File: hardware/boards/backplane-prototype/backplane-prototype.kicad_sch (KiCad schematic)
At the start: 32 parts, among them J1 DC_IN, J2 SLOT_1, J3 SLOT_2, J4 SLOT_3, J5 SLOT_4, J6 SLOT_5, J7 SLOT_6, J8 i2c_busses

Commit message: chore: checkpoint current board layout
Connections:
- net SCL_SLOT_1: now also D3.1 (IO1); no longer D3.2 (IO2)
- net SCL_SLOT_2: now also D4.1 (IO1); no longer D4.2 (IO2)
- net SCL_SLOT_3: now also D5.1 (IO1); no longer D5.2 (IO2)
- net SCL_SLOT_4: now also D6.1 (IO1); no longer D6.2 (IO2)
- net SCL_SLOT_5: now also D7.1 (IO1); no longer D7.2 (IO2)
- net SCL_SLOT_6: now also D8.1 (IO1); no longer D8.2 (IO2)
- net SDA_SLOT_1: now also D3.2 (IO2); no longer D3.1 (IO1)
- net SDA_SLOT_2: now also D4.2 (IO2); no longer D4.1 (IO1)
- net SDA_SLOT_3: now also D5.2 (IO2); no longer D5.1 (IO1)
- net SDA_SLOT_4: now also D6.2 (IO2); no longer D6.1 (IO1)
- net SDA_SLOT_5: now also D7.2 (IO2); no longer D7.1 (IO1)
- net SDA_SLOT_6: now also D8.2 (IO2); no longer D8.1 (IO1)
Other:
- title: Simplified XT30 Backplane Prototype -> Backplane Prototype
- moved on the sheet: J1, R10, R11, R12, R13, R14, R3, R4, R5, R6, R7, R8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

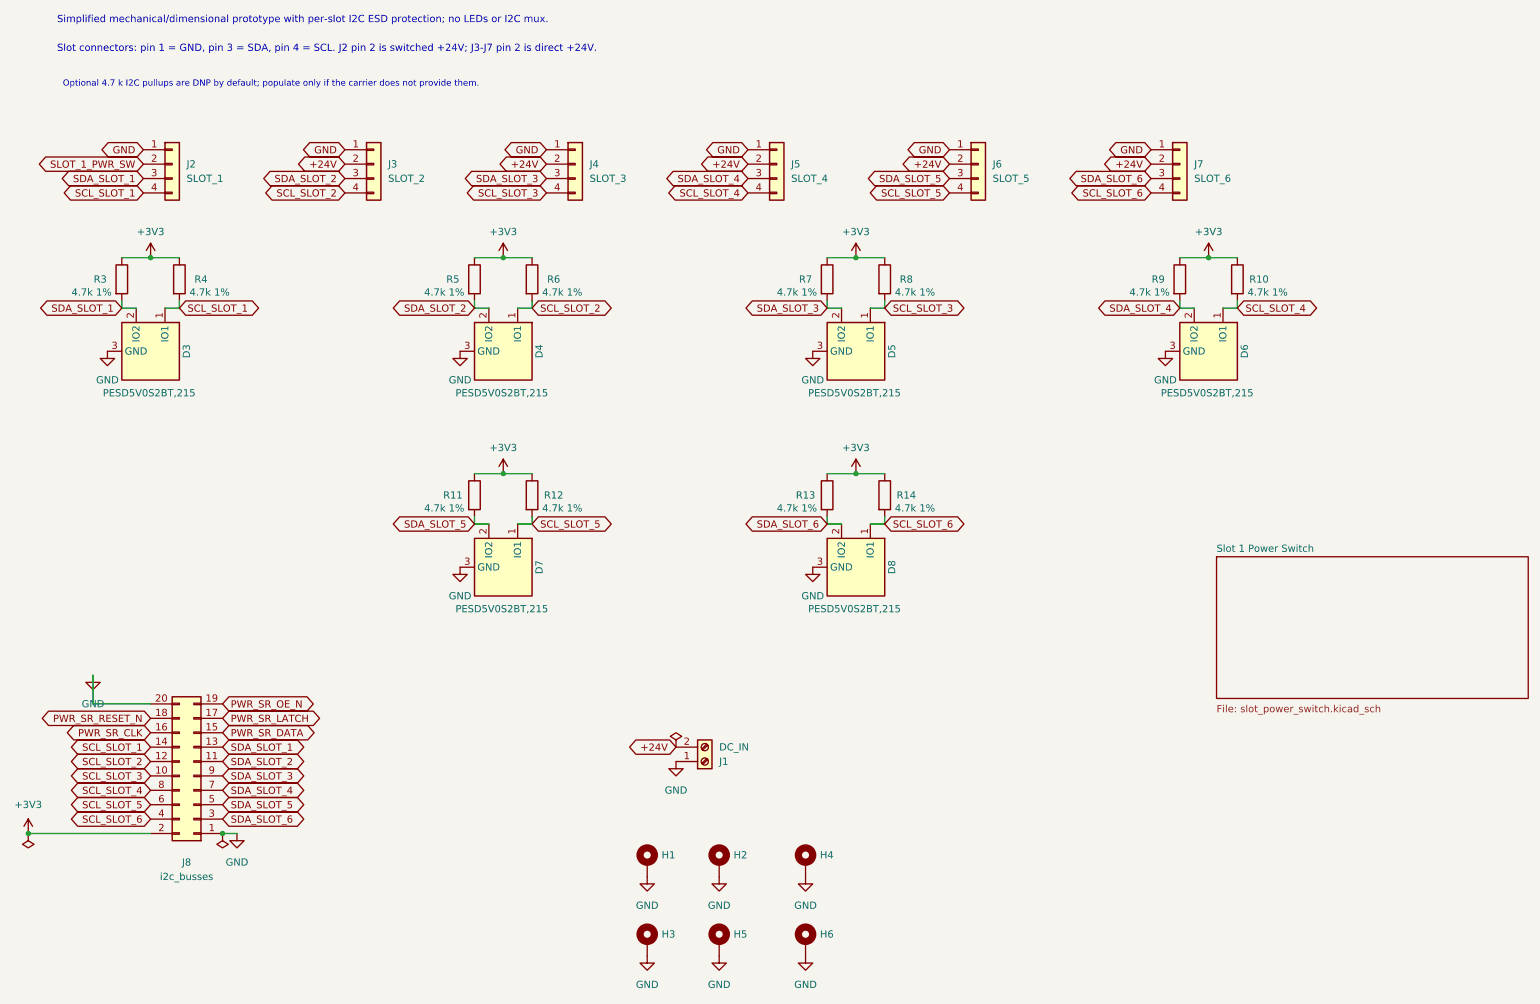
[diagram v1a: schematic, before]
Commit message: feat: add power switches for all backplane slots
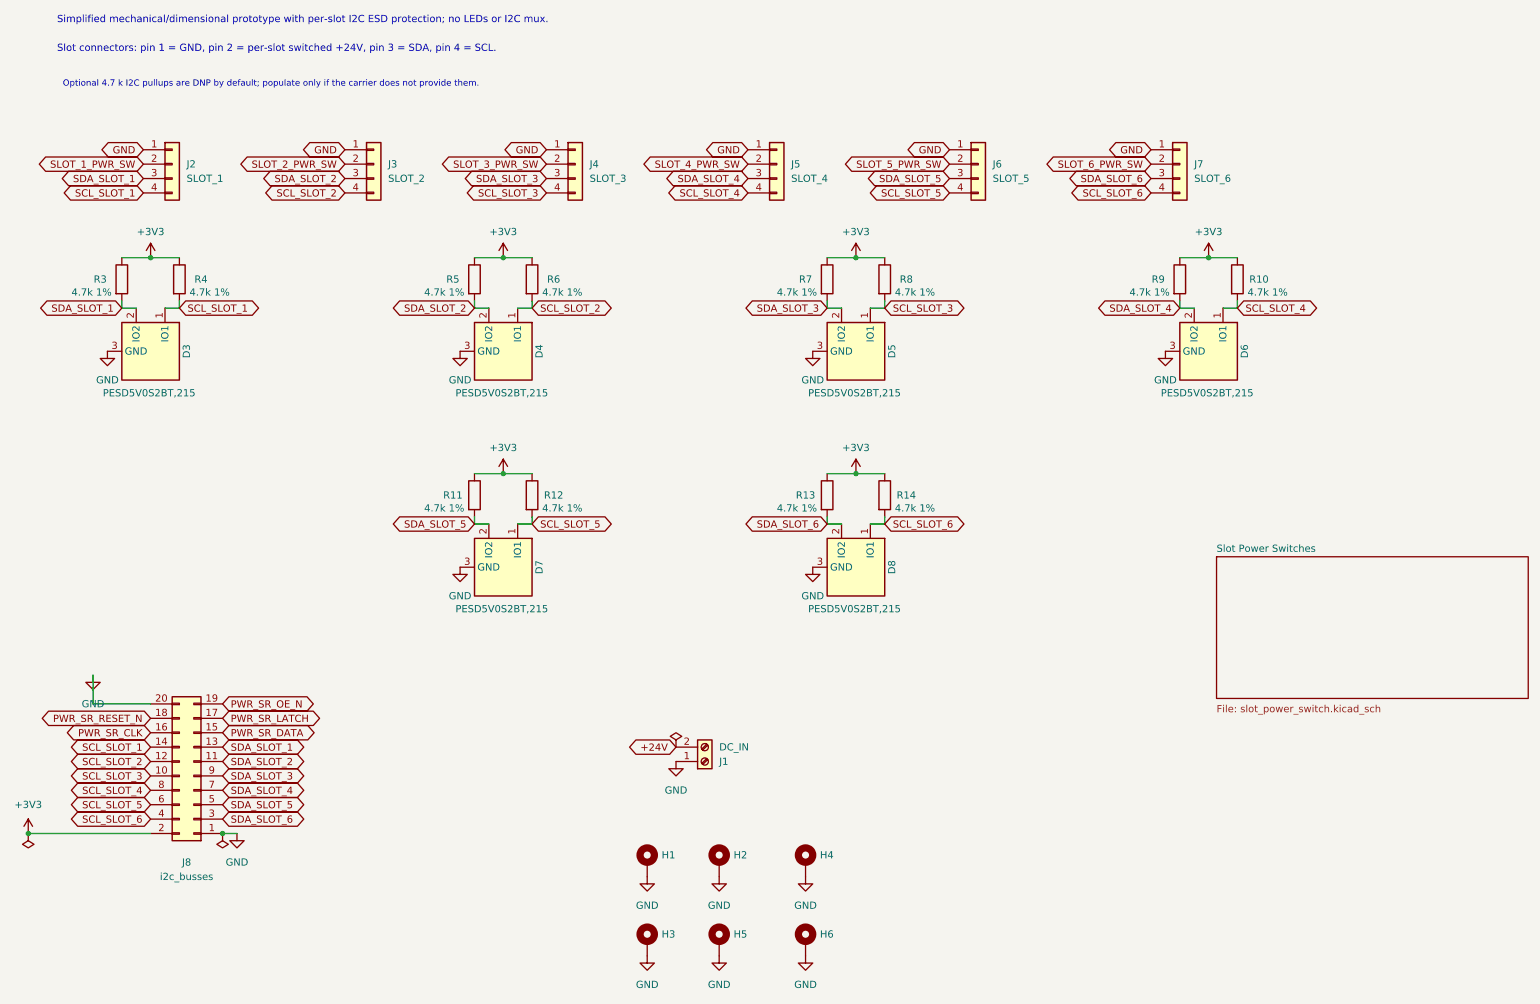
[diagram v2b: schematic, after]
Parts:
- J3: Pinout 1=GND; 2=+24V; 3=SDA; 4=SCL -> 1=GND; 2=SLOT_2_PWR_SW; 3=SDA; 4=SCL
- J4: Pinout 1=GND; 2=+24V; 3=SDA; 4=SCL -> 1=GND; 2=SLOT_3_PWR_SW; 3=SDA; 4=SCL
- J5: Pinout 1=GND; 2=+24V; 3=SDA; 4=SCL -> 1=GND; 2=SLOT_4_PWR_SW; 3=SDA; 4=SCL
- J6: Pinout 1=GND; 2=+24V; 3=SDA; 4=SCL -> 1=GND; 2=SLOT_5_PWR_SW; 3=SDA; 4=SCL
- J7: Pinout 1=GND; 2=+24V; 3=SDA; 4=SCL -> 1=GND; 2=SLOT_6_PWR_SW; 3=SDA; 4=SCL
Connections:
- net +24V: no longer J3.2 (Pin_2), J4.2 (Pin_2), J5.2 (Pin_2), J6.2 (Pin_2), J7.2 (Pin_2)
- new net SLOT_2_PWR_SW: J3.2 (Pin_2)
- new net SLOT_3_PWR_SW: J4.2 (Pin_2)
- new net SLOT_4_PWR_SW: J5.2 (Pin_2)
- new net SLOT_5_PWR_SW: J6.2 (Pin_2)
- new net SLOT_6_PWR_SW: J7.2 (Pin_2)
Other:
- sheet Slot 1 Power Switch renamed Slot Power Switches
- note added: "Slot connectors: pin 1 = GND, pin 2 = per-slot switched +24V, pin 3 = SDA, pin 4 = SCL."
- note removed: "Slot connectors: pin 1 = GND, pin 3 = SDA, pin 4 = SCL. J2 pin 2 is switched +24V; J3-J7 pin 2 is direct +24V."
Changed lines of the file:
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@@
 		)
 	)
-	(text "Slot connectors: pin 1 = GND, pin 3 = SDA, pin 4 = SCL. J2 pin 2 is switched +24V; J3-J7 pin 2 is direct +24V."
+	(text "Slot connectors: pin 1 = GND, pin 2 = per-slot switched +24V, pin 3 = SDA, pin 4 = SCL."
 		(exclude_from_sim no)
 		(at 25.4 25.4 0)
@@
 		)
 	)
-	(global_label "+24V"
+	(global_label "SLOT_3_PWR_SW"
 		(shape bidirectional)
 		(at 111.76 45.72 180)
@@
 		)
 	)
-	(global_label "+24V"
+	(global_label "SLOT_5_PWR_SW"
 		(shape bidirectional)
 		(at 182.88 45.72 180)
@@
 		)
 	)
-	(global_label "+24V"
+	(global_label "SLOT_4_PWR_SW"
 		(shape bidirectional)
 		(at 147.32 45.72 180)
@@
 		)
 	)
-	(global_label "+24V"
+	(global_label "SLOT_2_PWR_SW"
 		(shape bidirectional)
 		(at 76.2 45.72 180)
@@
 		)
 	)
-	(global_label "+24V"
+	(global_label "SLOT_6_PWR_SW"
 		(shape bidirectional)
 		(at 218.44 45.72 180)
@@
 			)
 		)
-		(property "Pinout" "1=GND; 2=+24V; 3=SDA; 4=SCL"
+		(property "Pinout" "1=GND; 2=SLOT_6_PWR_SW; 3=SDA; 4=SCL"
 			(at 223.52 45.72 0)
 			(hide yes)
@@
 			)
 		)
-		(property "Pinout" "1=GND; 2=+24V; 3=SDA; 4=SCL"
+		(property "Pinout" "1=GND; 2=SLOT_3_PWR_SW; 3=SDA; 4=SCL"
 			(at 116.84 45.72 0)
 			(hide yes)
@@
 			)
 		)
-		(property "Pinout" "1=GND; 2=+24V; 3=SDA; 4=SCL"
+		(property "Pinout" "1=GND; 2=SLOT_5_PWR_SW; 3=SDA; 4=SCL"
 			(at 187.96 45.72 0)
 			(hide yes)
@@
 			)
 		)
-		(property "Pinout" "1=GND; 2=+24V; 3=SDA; 4=SCL"
+		(property "Pinout" "1=GND; 2=SLOT_2_PWR_SW; 3=SDA; 4=SCL"
 			(at 81.28 45.72 0)
 			(hide yes)
@@
 			)
 		)
-		(property "Pinout" "1=GND; 2=+24V; 3=SDA; 4=SCL"
+		(property "Pinout" "1=GND; 2=SLOT_4_PWR_SW; 3=SDA; 4=SCL"
 			(at 152.4 45.72 0)
 			(hide yes)
@@
 			(color 0 0 0 0)
 		)
-		(property "Sheetname" "Slot 1 Power Switch"
+		(property "Sheetname" "Slot Power Switches"
 			(at 230 114.2884 0)
 			(show_name no)

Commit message: feat: replace backplane input terminal
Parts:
- J1: footprint mini-rack-power:DEGSON_DG135T-10.16-02P -> mini-rack-power:DORABO_DB910-6.35-2P-GN-S; LCSC (none) -> C395872; MPN (none) -> DB910-6.35-2P-GN-S; Manufacturer (none) -> DORABO
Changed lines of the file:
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@@
 			)
 		)
-		(property "Footprint" "mini-rack-power:DEGSON_DG135T-10.16-02P"
+		(property "Footprint" "mini-rack-power:DORABO_DB910-6.35-2P-GN-S"
 			(at 139.7 151.13 0)
 			(hide yes)
@@
 			)
 		)
-		(property "Datasheet" ""
+		(property "Datasheet" "https://www.lcsc.com/datasheet/C395872.pdf"
 			(at 139.7 151.13 0)
 			(hide yes)
@@
 			)
 		)
-		(property "Description" "Prototype main DC input screw terminal"
+		(property "Description" "DORABO DB910-6.35-2P-GN-S, 2-position 6.35 mm pitch vertical screw terminal, LCSC C395872"
 			(at 139.7 151.13 0)
 			(hide yes)
@@
 			(at 139.7 151.13 0)
 			(hide yes)
+			(show_name no)
+			(do_not_autoplace no)
+			(effects
+				(font
+					(size 1.27 1.27)
+				)
+			)
+		)
+		(property "MPN" "DB910-6.35-2P-GN-S"
+			(at 139.7 151.13 0)
+			(hide yes)
+			(show_name no)
+			(do_not_autoplace no)
+			(effects
+				(font
+					(size 1.27 1.27)
+				)
+			)
+		)
+		(property "LCSC" "C395872"
+			(at 139.7 151.13 0)
+			(hide yes)
+			(show_name no)
+			(do_not_autoplace no)
+			(effects
+				(font
+					(size 1.27 1.27)
+				)
+			)
+		)
+		(property "Manufacturer" "DORABO"
+			(at 139.7 151.13 0)
+			(hide yes)

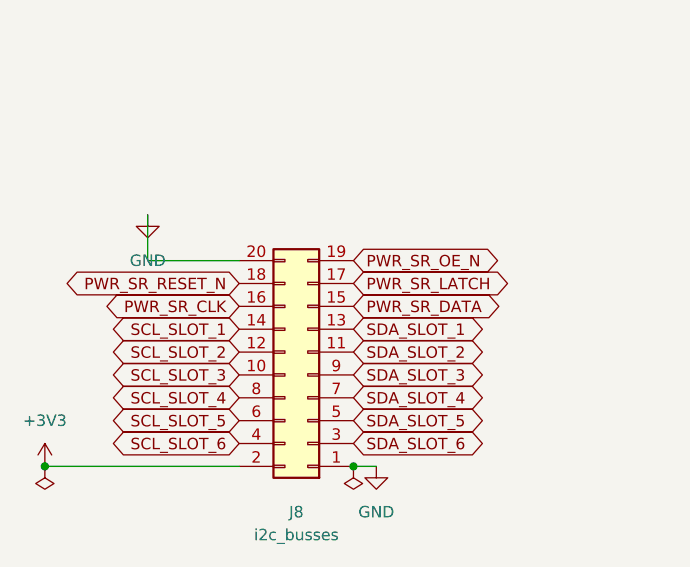
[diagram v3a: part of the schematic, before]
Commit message: Replace slot power shift register with PCA9554
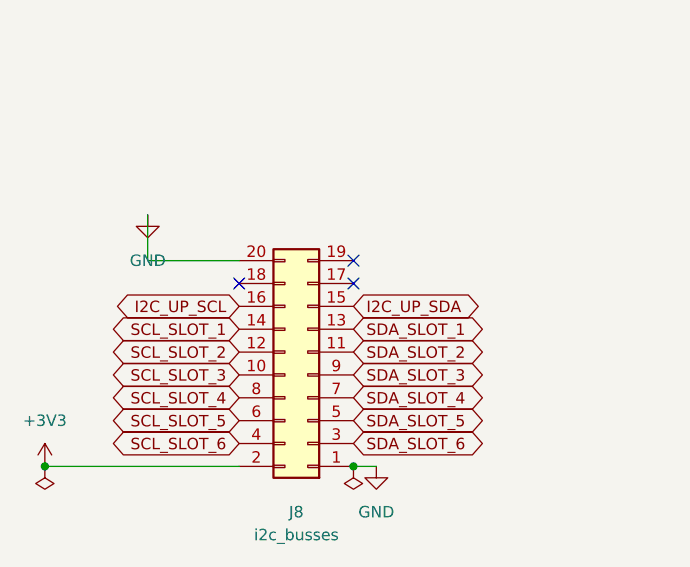
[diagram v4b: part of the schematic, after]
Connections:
- net PWR_SR_CLK renamed I2C_UP_SCL
- net PWR_SR_DATA renamed I2C_UP_SDA
- net PWR_SR_LATCH: no longer names the net of J8.17 (Pin_17)
- net PWR_SR_OE_N: no longer names the net of J8.19 (Pin_19)
- net PWR_SR_RESET_N: no longer names the net of J8.18 (Pin_18)
- no-connect marks 0 -> 3
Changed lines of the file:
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@@
-		)
-	)
-	(global_label "PWR_SR_OE_N"
-		(shape bidirectional)
-		(at 54.61 140.97 0)
-		(effects
-			(font
-				(size 1.27 1.27)
-			)
-			(justify left)
-		)
-		(property "Intersheetrefs" "${INTERSHEET_REFS}"
-			(at 54.61 140.97 0)
-			(hide yes)
-			(show_name no)
-			(do_not_autoplace no)
-			(effects
-				(font
-					(size 1.27 1.27)
-				)
-			)
 		)
 	)
@@
 		)
 	)
-	(global_label "PWR_SR_DATA"
+	(global_label "I2C_UP_SDA"
 		(shape bidirectional)
 		(at 54.61 146.05 0)
@@
 		)
 	)
-	(global_label "PWR_SR_LATCH"
-		(shape bidirectional)
-		(at 54.61 143.51 0)
-		(effects
-			(font
-				(size 1.27 1.27)
-			)
-			(justify left)
-		)
-		(property "Intersheetrefs" "${INTERSHEET_REFS}"
-			(at 54.61 143.51 0)
-			(hide yes)
-			(show_name no)
-			(do_not_autoplace no)
-			(effects
-				(font
-					(size 1.27 1.27)
-				)
-			)
-		)
-	)
 	(global_label "SDA_SLOT_6"
 		(shape bidirectional)
@@
 		)
 	)
-	(global_label "PWR_SR_CLK"
+	(global_label "I2C_UP_SCL"
 		(shape bidirectional)
 		(at 41.91 146.05 180)
@@
 		)
 	)
-	(global_label "PWR_SR_RESET_N"
-		(shape bidirectional)
-		(at 41.91 143.51 180)
-		(effects
-			(font
-				(size 1.27 1.27)
-			)
-			(justify right)
-		)
-		(property "Intersheetrefs" "${INTERSHEET_REFS}"
-			(at 41.91 143.51 0)
-			(hide yes)
-			(show_name no)
-			(do_not_autoplace no)
-			(effects
-				(font
-					(size 1.27 1.27)
-				)
-			)
-		)
-	)
 	(global_label "SCL_SLOT_5"
 		(shape bidirectional)
@@
 		)
 	)
+		(no_connect
+		(at 54.61 140.97)
+	)
+	(no_connect
+		(at 54.61 143.51)
+	)
+	(no_connect
+		(at 41.91 143.51)
+	)
 	(symbol

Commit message: Checkpoint: pre-autoroute
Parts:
- renumbered D3 to D1, D4 to D2, D7 to D3, D5 to D4, D8 to D5, H3 to H2, H2 to H3, H5 to H4, H4 to H5, J2 to J1, J8 to J2, J1 to J5, J5 to J6, J6 to J7, J7 to J8, R3 to R1, R14 to R10, R9 to R11, R10 to R12, R4 to R2, R5 to R3, R11 to R4, R6 to R5, R12 to R6, R13 to R8, R8 to R9
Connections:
- net SCL_SLOT_1: no longer J2.14 (Pin_14)
- net SCL_SLOT_2: no longer J2.12 (Pin_12)
- net SCL_SLOT_3: no longer J2.10 (Pin_10)
- net SCL_SLOT_4: no longer J2.8 (Pin_8)
- net SCL_SLOT_5: no longer J2.6 (Pin_6)
- net SCL_SLOT_6: no longer J2.4 (Pin_4)
- net SDA_SLOT_1: no longer J2.13 (Pin_13)
- net SDA_SLOT_2: no longer J2.11 (Pin_11)
- net SDA_SLOT_3: no longer J2.9 (Pin_9)
- net SDA_SLOT_4: no longer J2.7 (Pin_7)
- net SDA_SLOT_5: no longer J2.5 (Pin_5)
- net SDA_SLOT_6: no longer J2.3 (Pin_3)
- no-connect marks 3 -> 15
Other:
- note added: "Backplane prototype with per-slot I2C ESD protection and TCA9548A bus multiplexing; no LEDs."
- note added: "Per-slot 4.7 k I2C pullups bias each isolated TCA9548A channel after the slot ESD protection."
- note added: "Slot connectors: pin 1 = GND, pin 2 = per-slot switched +24V, pin 3 = SDA, pin 4 = SCL. J8 pins 15/16 carry upstream SDA/SCL; pins 3-14 and 17-19 are spare."
- note removed: "Optional 4.7 k I2C pullups are DNP by default; populate only if the carrier does not provide them."
- note removed: "Simplified mechanical/dimensional prototype with per-slot I2C ESD protection; no LEDs or I2C mux."
- note removed: "Slot connectors: pin 1 = GND, pin 2 = per-slot switched +24V, pin 3 = SDA, pin 4 = SCL."

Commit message: Checkpoint before auto-router
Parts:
- J2: value i2c_busses -> i2c_backpack; footprint Connector_PinHeader_1.00mm:PinHeader_2x10_P1.00mm_Vertical -> Connector_PinHeader_2.54mm:PinHeader_2x03_P2.54mm_Vertical; symbol Connector_Generic:Conn_02x10_Odd_Even -> Connector_Generic:Conn_02x03_Odd_Even
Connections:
- net +3V3: now also J2.4 (Pin_4)
- net GND: now also J2.3 (Pin_3); no longer J2.20 (Pin_20)
- net I2C_UP_SCL: now also J2.6 (Pin_6); no longer J2.16 (Pin_16)
- net I2C_UP_SDA: now also J2.5 (Pin_5); no longer J2.15 (Pin_15)
- no-connect marks 15 -> 0

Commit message: Checkpoint before auto-router
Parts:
- H4: now not fitted
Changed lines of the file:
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@@
 		(on_board yes)
 		(in_pos_files yes)
-		(dnp no)
+		(dnp yes)
 		(fields_autoplaced yes)
 		(property "Reference" "H4"
